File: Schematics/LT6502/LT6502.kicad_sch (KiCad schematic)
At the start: 36 parts, among them SW1 SW_Omron_B3FS, U1 TC1232, U2 W65C02S6TQG-14, U3 IS62C256AL, U4 IS62C256AL, U5 SST39SF010

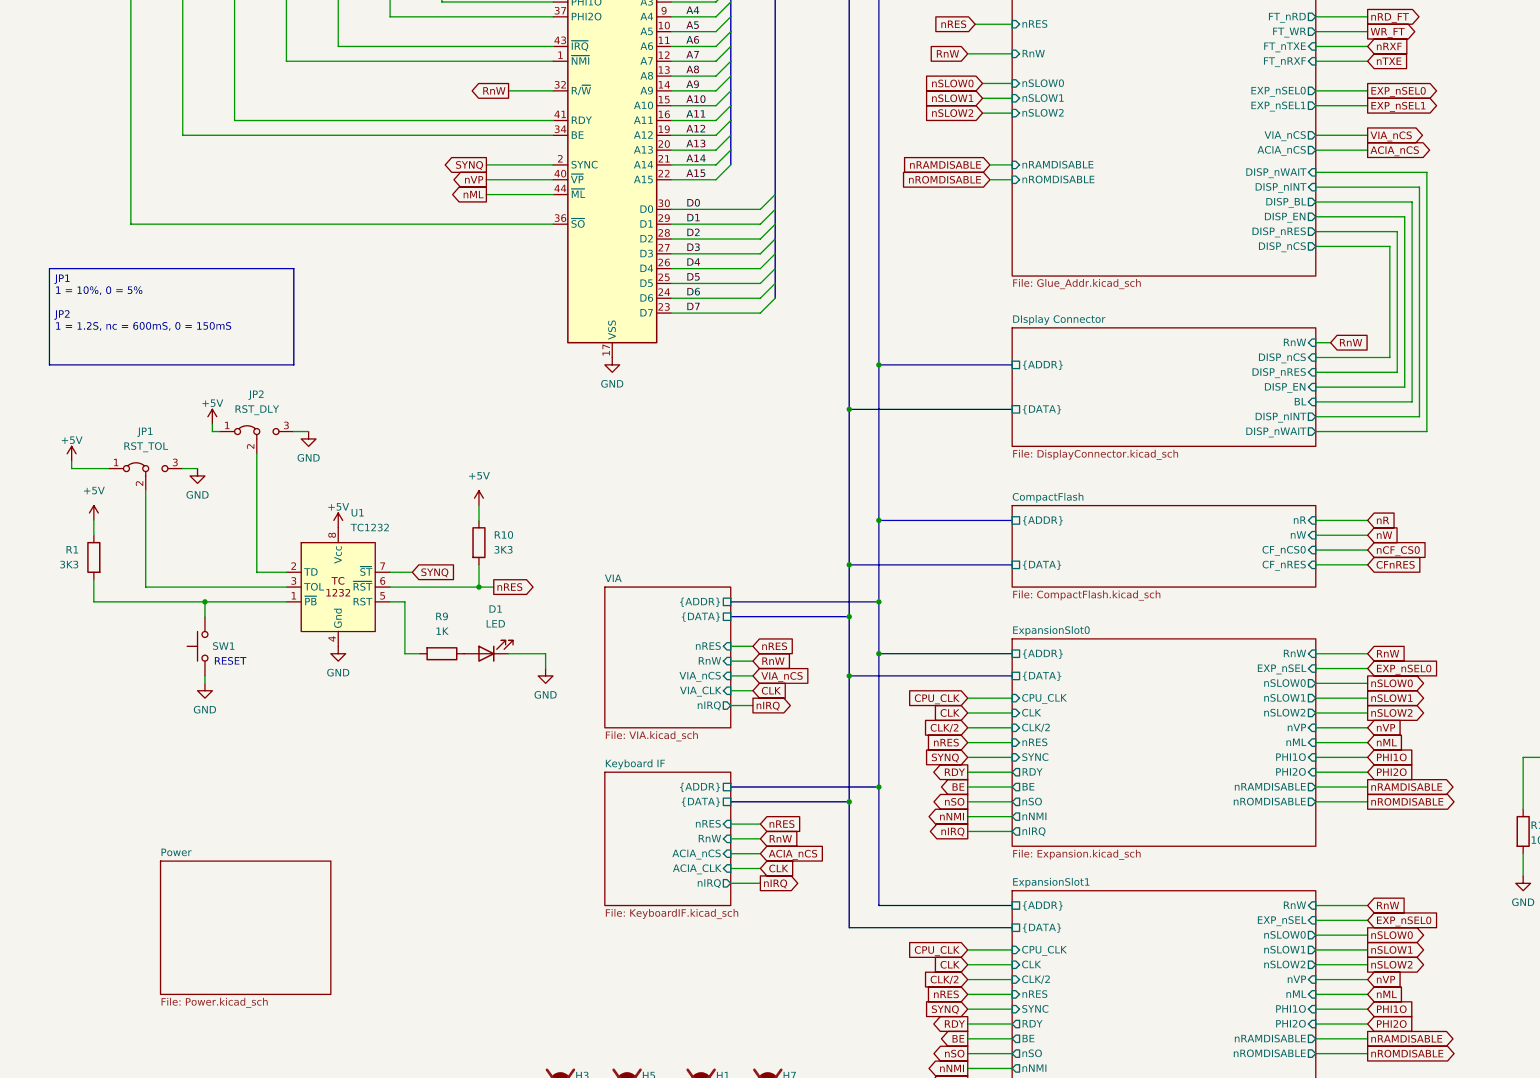
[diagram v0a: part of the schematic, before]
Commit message: Tweaks to Schematics
Shrunk main PCB
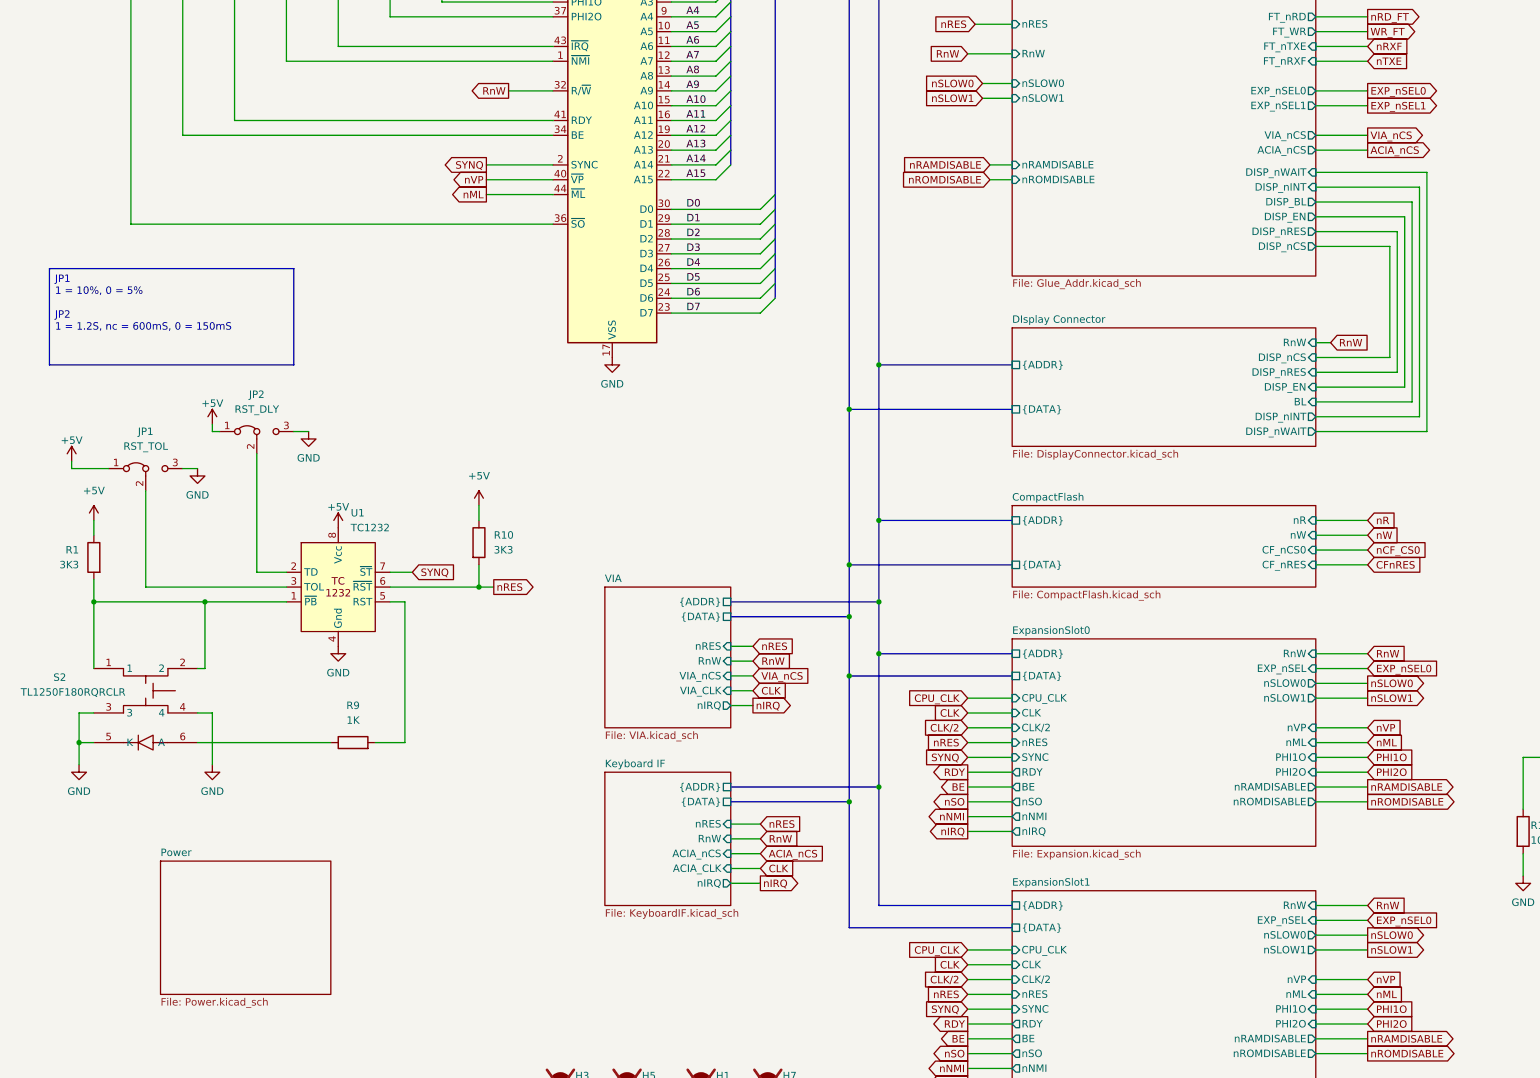
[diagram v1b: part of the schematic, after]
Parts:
- removed D1: LED, LED_SMD:LED_0603_1608Metric, symbol Device:LED
- removed SW1: SW_Omron_B3FS, Button_Switch_SMD:SW_SPST_Omron_B3FS-105xP, symbol Switch:SW_Omron_B3FS
- added S2: TL1250F180RQRCLR, TL1250F180RQRCLR:TL1250F180RQRCLR, symbol TL1250F180RQRCLR:TL1250F180RQRCLR
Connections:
- net GND: now also S2.3, S2.4, S2.5 (K)
- net at R1.2, U1.1 (~{PB}): now also S2.1, S2.2
- net at R9.1: now also S2.6 (A)
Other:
- sheet ExpansionSlot0 ports: added none; removed nSLOW2
- sheet ExpansionSlot1 ports: added none; removed nSLOW2
- sheet Glue_Addr ports: added none; removed nSLOW2
- note removed: "RESET"
- moved on the sheet: R9

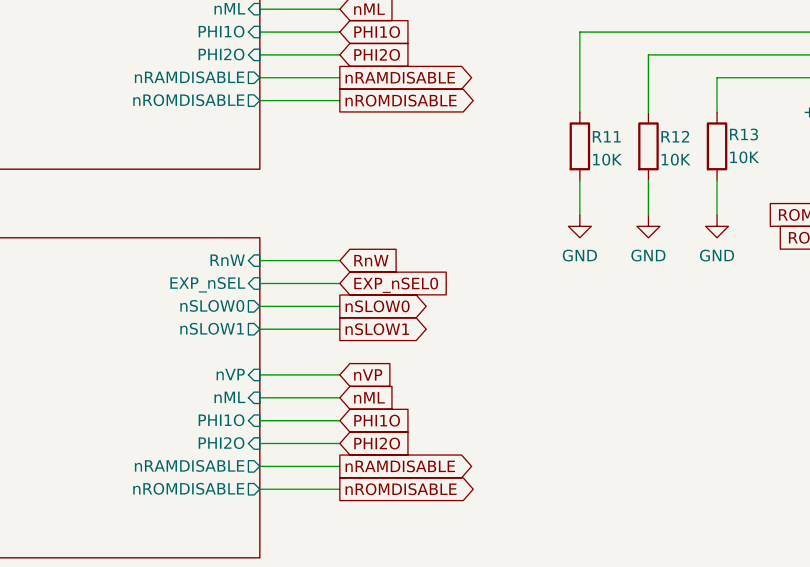
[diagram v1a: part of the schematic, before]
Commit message: Further work on Schematics, All parts placed on PCB
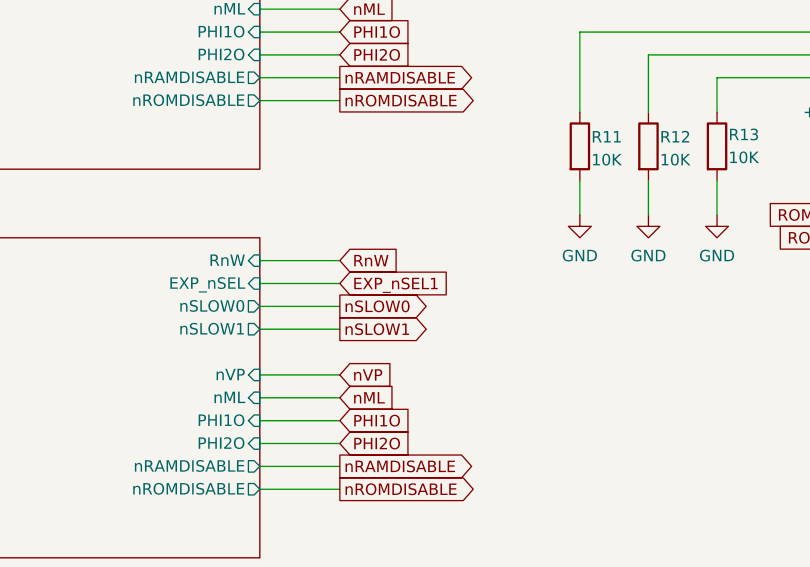
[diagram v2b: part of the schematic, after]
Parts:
- R1, R10, R11, R12, R13, R2, R3, R4, R5, R6, R7, R8, R9: footprint Resistor_SMD:R_0603_1608Metric_Pad0.98x0.95mm_HandSolder -> Resistor_SMD:R_0402_1005Metric
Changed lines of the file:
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@@
 		)
 	)
-	(global_label "EXP_nSEL0"
+	(global_label "EXP_nSEL1"
 		(shape input)
 		(at 251.46 224.79 0)
@@
 			)
 		)
-		(property "Footprint" "Resistor_SMD:R_0603_1608Metric_Pad0.98x0.95mm_HandSolder"
+		(property "Footprint" "Resistor_SMD:R_0402_1005Metric"
 			(at 34.798 162.56 90)
 			(effects
@@
 			)
 		)
-		(property "Footprint" "Resistor_SMD:R_0603_1608Metric_Pad0.98x0.95mm_HandSolder"
+		(property "Footprint" "Resistor_SMD:R_0402_1005Metric"
 			(at 55.372 38.1 90)
 			(effects
@@
 			)
 		)
-		(property "Footprint" "Resistor_SMD:R_0603_1608Metric_Pad0.98x0.95mm_HandSolder"
+		(property "Footprint" "Resistor_SMD:R_0402_1005Metric"
 			(at 283.972 209.55 90)
 			(effects
@@
 			)
 		)
-		(property "Footprint" "Resistor_SMD:R_0603_1608Metric_Pad0.98x0.95mm_HandSolder"
+		(property "Footprint" "Resistor_SMD:R_0402_1005Metric"
 			(at 77.47 196.088 90)
 			(effects
@@
 			)
 		)
-		(property "Footprint" "Resistor_SMD:R_0603_1608Metric_Pad0.98x0.95mm_HandSolder"
+		(property "Footprint" "Resistor_SMD:R_0402_1005Metric"
 			(at 46.482 38.1 90)
 			(effects
@@
 			)
 		)
-		(property "Footprint" "Resistor_SMD:R_0603_1608Metric_Pad0.98x0.95mm_HandSolder"
+		(property "Footprint" "Resistor_SMD:R_0402_1005Metric"
 			(at 64.262 38.1 90)
 			(effects
@@
 			)
 		)
-		(property "Footprint" "Resistor_SMD:R_0603_1608Metric_Pad0.98x0.95mm_HandSolder"
+		(property "Footprint" "Resistor_SMD:R_0402_1005Metric"
 			(at 37.592 38.1 90)
 			(effects
@@
 			)
 		)
-		(property "Footprint" "Resistor_SMD:R_0603_1608Metric_Pad0.98x0.95mm_HandSolder"
+		(property "Footprint" "Resistor_SMD:R_0402_1005Metric"
 			(at 276.352 209.55 90)
 			(effects
@@
 			)
 		)
-		(property "Footprint" "Resistor_SMD:R_0603_1608Metric_Pad0.98x0.95mm_HandSolder"
+		(property "Footprint" "Resistor_SMD:R_0402_1005Metric"
 			(at 90.932 38.1 90)
 			(effects
@@
 			)
 		)
-		(property "Footprint" "Resistor_SMD:R_0603_1608Metric_Pad0.98x0.95mm_HandSolder"
+		(property "Footprint" "Resistor_SMD:R_0402_1005Metric"
 			(at 73.152 38.1 90)
 			(effects
@@
 			)
 		)
-		(property "Footprint" "Resistor_SMD:R_0603_1608Metric_Pad0.98x0.95mm_HandSolder"
+		(property "Footprint" "Resistor_SMD:R_0402_1005Metric"
 			(at 82.042 38.1 90)
 			(effects
@@
 			)
 		)
-		(property "Footprint" "Resistor_SMD:R_0603_1608Metric_Pad0.98x0.95mm_HandSolder"
+		(property "Footprint" "Resistor_SMD:R_0402_1005Metric"
 			(at 291.592 209.55 90)
 			(effects
@@
 			)
 		)
-		(property "Footprint" "Resistor_SMD:R_0603_1608Metric_Pad0.98x0.95mm_HandSolder"
+		(property "Footprint" "Resistor_SMD:R_0402_1005Metric"
 			(at 97.282 160.02 90)
 			(effects

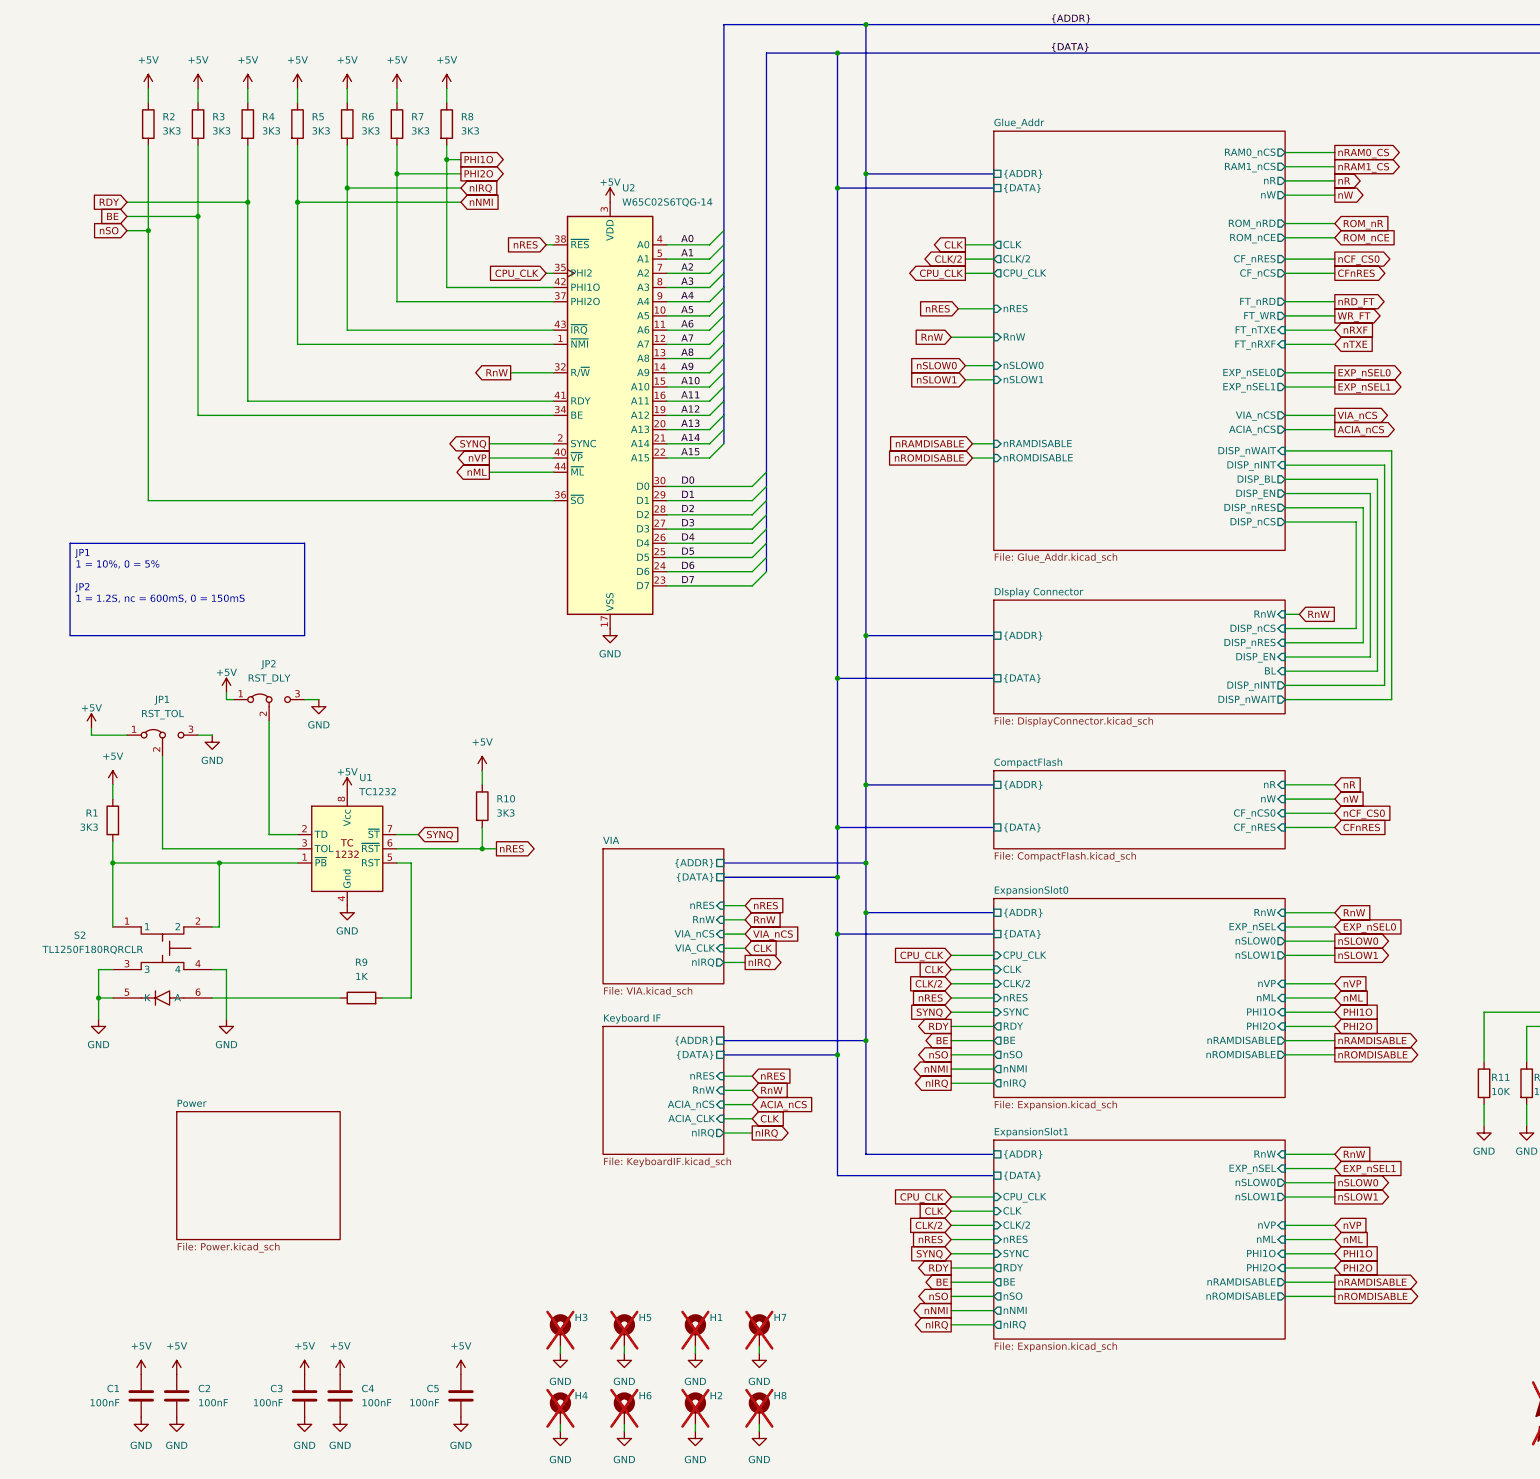
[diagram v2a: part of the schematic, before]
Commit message: Updated main board and started keybed
main board a bit wider due to keybed width
created keybed, begun routing
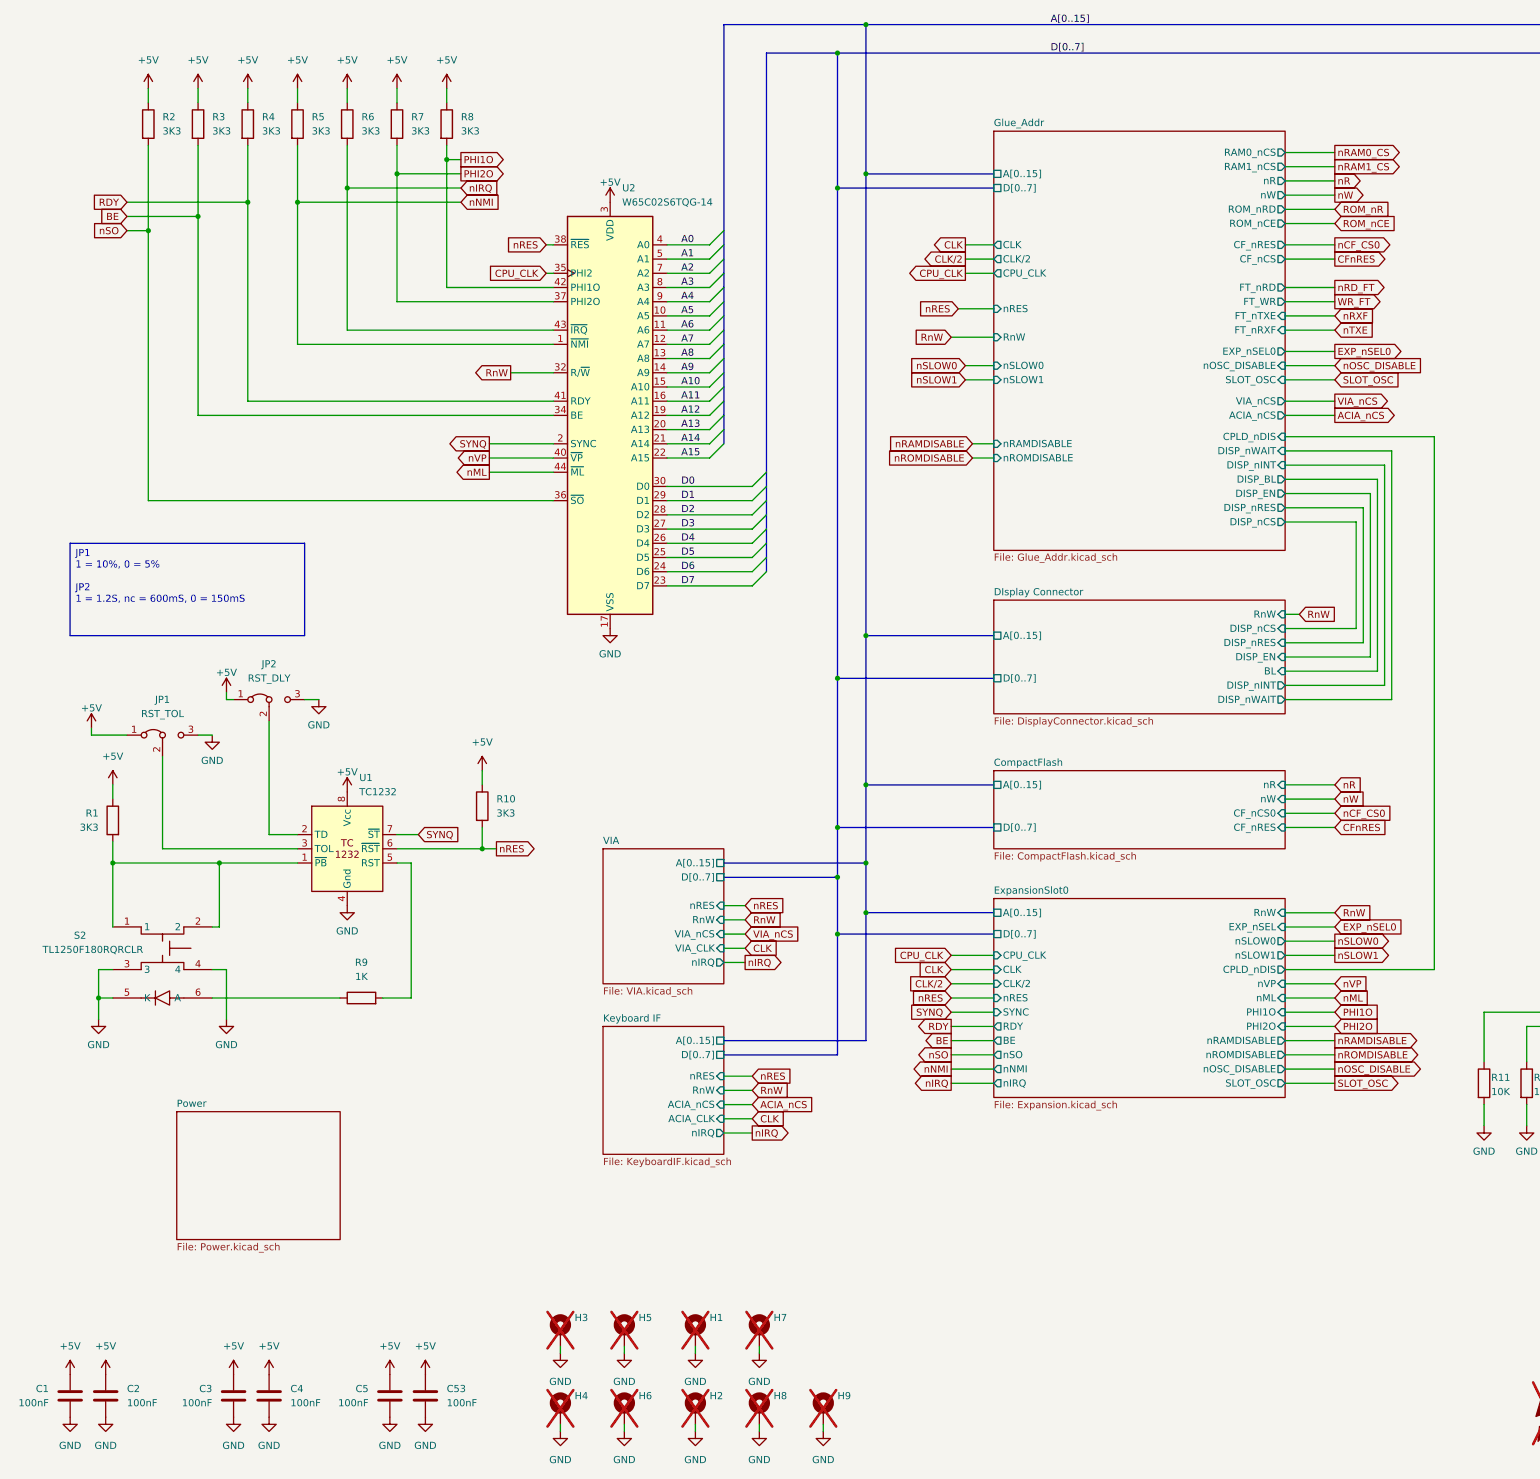
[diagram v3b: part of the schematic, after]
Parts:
- added C53: 100nF, Capacitor_SMD:C_0603_1608Metric, symbol Device:C
- added H9: MountingHole_Pad, MountingHole:MountingHole_3.2mm_M3_Pad_TopBottom, symbol Mechanical:MountingHole_Pad
- U1: Mouser Part Number (none) -> 579-TC1232CPA
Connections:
- net +5V: now also C53.1
- net GND: now also C53.2, H9.1
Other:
- removed sheet ExpansionSlot1
- sheet CompactFlash ports: added A[0..15], D[0..7]; removed {ADDR}, {DATA}
- sheet DIsplay Connector ports: added A[0..15], D[0..7]; removed {ADDR}, {DATA}
- sheet ExpansionSlot0 ports: added A[0..15], CPLD_nDIS, D[0..7], SLOT_OSC, nOSC_DISABLE; removed {ADDR}, {DATA}
- sheet Glue_Addr ports: added A[0..15], CPLD_nDIS, D[0..7], SLOT_OSC, nOSC_DISABLE; removed EXP_nSEL1, {ADDR}, {DATA}
- sheet Keyboard IF ports: added A[0..15], D[0..7]; removed {ADDR}, {DATA}
- sheet VIA ports: added A[0..15], D[0..7]; removed {ADDR}, {DATA}
- moved on the sheet: C1, C2, C3, C4, C5
